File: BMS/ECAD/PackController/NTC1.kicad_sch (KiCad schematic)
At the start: 3 parts

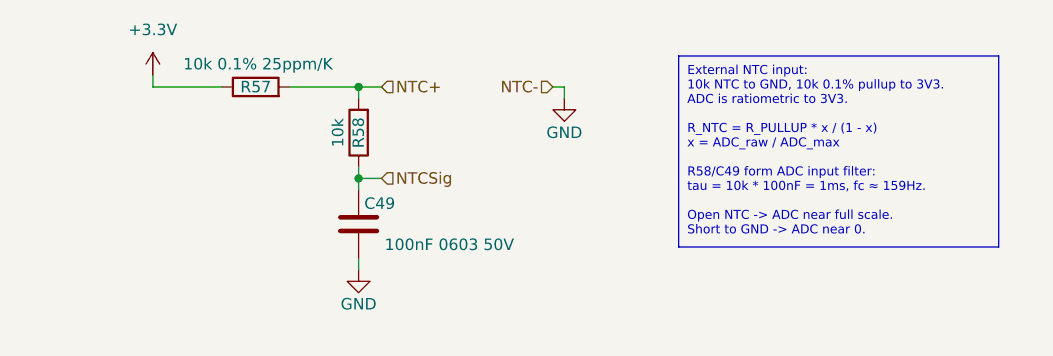
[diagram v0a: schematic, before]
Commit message: close to finish BMS master, only some footprints needed
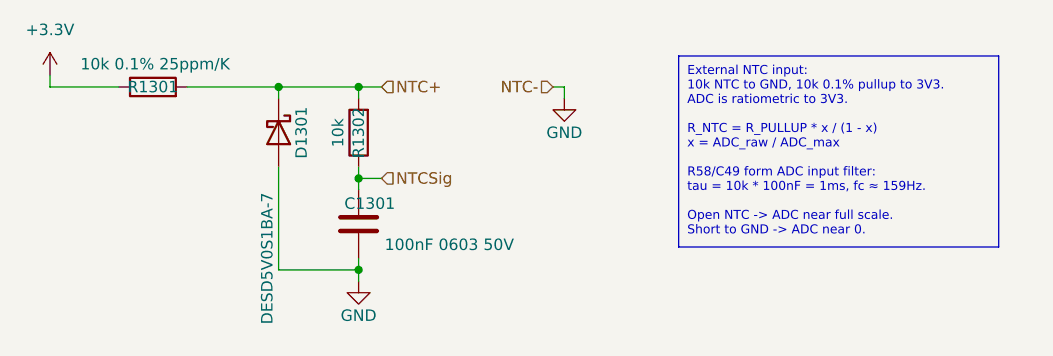
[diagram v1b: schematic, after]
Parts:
- added D1301: DESD5V0S1BA-7, Diode_SMD:D_SOD-323, symbol Device:D_Schottky
- renumbered C49 to C1301, R57 to R1301, R58 to R1302
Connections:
- net GND: now also D1301.2 (A)
- net NTC+: now also D1301.1 (K)
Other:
- moved on the sheet: R1301
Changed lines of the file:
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@@
+	)
+	(junction
+		(at 124.46 85.09)
+		(diameter 0)
+		(color 0 0 0 0)
 	)
 	(junction
@@
 		(color 0 0 0 0)
 	)
-	(wire
-		(pts
-			(xy 110.49 85.09) (xy 110.49 83.82)
+	(junction
+		(at 133.35 105.41)
+		(diameter 0)
+		(color 0 0 0 0)
+	)
+	(wire
+		(pts
+			(xy 99.06 85.09) (xy 99.06 83.82)
 		)
 		(stroke
@@
 	(wire
 		(pts
+			(xy 124.46 105.41) (xy 133.35 105.41)
+		)
+		(stroke
+			(width 0)
+			(type default)
+		)
+	)
+	(wire
+		(pts
+			(xy 124.46 85.09) (xy 124.46 86.36)
+		)
+		(stroke
+			(width 0)
+			(type default)
+		)
+	)
+	(wire
+		(pts
 			(xy 156.21 85.09) (xy 156.21 86.36)
 		)
@@
 	(wire
 		(pts
-			(xy 125.73 85.09) (xy 133.35 85.09)
+			(xy 124.46 85.09) (xy 133.35 85.09)
+		)
+		(stroke
+			(width 0)
+			(type default)
+		)
+	)
+	(wire
+		(pts
+			(xy 133.35 106.68) (xy 133.35 105.41)
+		)
+		(stroke
+			(width 0)
+			(type default)
+		)
+	)
+	(wire
+		(pts
+			(xy 114.3 85.09) (xy 124.46 85.09)
 		)
 		(stroke
@@
 	(wire
 		(pts
-			(xy 110.49 85.09) (xy 118.11 85.09)
+			(xy 124.46 93.98) (xy 124.46 105.41)
+		)
+		(stroke
+			(width 0)
+			(type default)
+		)
+	)
+	(wire
+		(pts
+			(xy 99.06 85.09) (xy 106.68 85.09)
 		)
 		(stroke
@@
 	(symbol
 		(lib_id "Device:R")
-		(at 121.92 85.09 90)
+		(at 110.49 85.09 90)
 		(unit 1)
 		(body_style 1)
@@
 		(in_pos_files yes)
 		(dnp no)
-		(property "Reference" "R57"
-			(at 121.92 85.09 90)
+		(property "Reference" "R1301"
+			(at 110.49 85.09 90)
 			(show_name no)
 			(do_not_autoplace no)
@@
 		)
 		(property "Value" "10k 0.1% 25ppm/K"
-			(at 122.174 82.55 90)
+			(at 110.744 82.55 90)
 			(show_name no)
 			(do_not_autoplace no)
@@
 		)
 		(property "Footprint" "Resistor_SMD:R_0603_1608Metric_Pad0.98x0.95mm_HandSolder"
-			(at 121.92 86.868 90)
+			(at 110.49 86.868 90)
 			(hide yes)
 			(show_name no)
@@
 		)
 		(property "Datasheet" ""
-			(at 121.92 85.09 0)
+			(at 110.49 85.09 0)
 			(hide yes)
 			(show_name no)
@@
 		)
 		(property "Description" ""
-			(at 121.92 85.09 0)
+			(at 110.49 85.09 0)
 			(show_name no)
 			(do_not_autoplace no)
@@
 			(project "Pack_Controller"
 				(path "/58a1c93e-baba-4d23-9191-955e00968735/45830960-bd48-4e73-a3a7-091edb18d6d3/71e65725-80b2-472c-8002-e08c907aa751"
-					(reference "R71")
+					(reference "R1401")
 					(unit 1)
 				)
 				(path "/58a1c93e-baba-4d23-9191-955e00968735/45830960-bd48-4e73-a3a7-091edb18d6d3/bb3a350a-a658-4971-83cd-58f1dca54bb5"
-					(reference "R73")
+					(reference "R1501")
 					(unit 1)
 				)
 				(path "/58a1c93e-baba-4d23-9191-955e00968735/45830960-bd48-4e73-a3a7-091edb18d6d3/f34c3682-d9f6-426f-8996-e47c99f84a0f"
-					(reference "R57")
+					(reference "R1301")
 					(unit 1)
 				)
@@
 		(in_pos_files yes)
 		(dnp no)
-		(property "Reference" "R58"
+		(property "Reference" "R1302"
 			(at 133.35 90.17 90)
 			(show_name no)
@@
 			(project "Pack_Controller"
 				(path "/58a1c93e-baba-4d23-9191-955e00968735/45830960-bd48-4e73-a3a7-091edb18d6d3/71e65725-80b2-472c-8002-e08c907aa751"
-					(reference "R72")
+					(reference "R1402")
 					(unit 1)
 				)
 				(path "/58a1c93e-baba-4d23-9191-955e00968735/45830960-bd48-4e73-a3a7-091edb18d6d3/bb3a350a-a658-4971-83cd-58f1dca54bb5"
-					(reference "R74")
+					(reference "R1502")
 					(unit 1)
 				)
 				(path "/58a1c93e-baba-4d23-9191-955e00968735/45830960-bd48-4e73-a3a7-091edb18d6d3/f34c3682-d9f6-426f-8996-e47c99f84a0f"
-					(reference "R58")
+					(reference "R1302")
 					(unit 1)
 				)
@@
 		(in_pos_files yes)
 		(dnp no)
-		(property "Reference" "C49"
+		(property "Reference" "C1301"
 			(at 137.414 98.044 0)
 			(show_name no)
@@
 			(project "Pack_Controller"
 				(path "/58a1c93e-baba-4d23-9191-955e00968735/45830960-bd48-4e73-a3a7-091edb18d6d3/71e65725-80b2-472c-8002-e08c907aa751"
-					(reference "C50")
+					(reference "C1401")
 					(unit 1)
 				)
 				(path "/58a1c93e-baba-4d23-9191-955e00968735/45830960-bd48-4e73-a3a7-091edb18d6d3/bb3a350a-a658-4971-83cd-58f1dca54bb5"
-					(reference "C51")
+					(reference "C1501")
 					(unit 1)
 				)
 				(path "/58a1c93e-baba-4d23-9191-955e00968735/45830960-bd48-4e73-a3a7-091edb18d6d3/f34c3682-d9f6-426f-8996-e47c99f84a0f"
-					(reference "C49")
+					(reference "C1301")
 					(unit 1)
 				)
@@
 	(symbol
 		(lib_id "power:GND")
-		(at 133.35 105.41 0)
+		(at 133.35 106.68 0)
 		(unit 1)
 		(body_style 1)
@@
 		(in_pos_files yes)
 		(dnp no)
-		(property "Reference" "#PWR061"
-			(at 133.35 111.76 0)
+		(property "Reference" "#PWR01303"
+			(at 133.35 113.03 0)
 			(hide yes)
 			(show_name no)
@@
 		)
 		(property "Value" "GND"
-			(at 133.35 109.22 0)
+			(at 133.35 110.49 0)
 			(show_name no)
 			(do_not_autoplace no)
@@
 		)
 		(property "Footprint" ""
-			(at 133.35 105.41 0)
+			(at 133.35 106.68 0)
 			(hide yes)
 			(show_name no)
@@
 		)
 		(property "Datasheet" ""
-			(at 133.35 105.41 0)
+			(at 133.35 106.68 0)
 			(hide yes)
 			(show_name no)
@@
 		)
 		(property "Description" ""
-			(at 133.35 105.41 0)
+			(at 133.35 106.68 0)
 			(show_name no)
 			(do_not_autoplace no)
@@
 			(project "Pack_Controller"
 				(path "/58a1c93e-baba-4d23-9191-955e00968735/45830960-bd48-4e73-a3a7-091edb18d6d3/71e65725-80b2-472c-8002-e08c907aa751"
-					(reference "#PWR063")
+					(reference "#PWR01403")
 					(unit 1)
 				)
 				(path "/58a1c93e-baba-4d23-9191-955e00968735/45830960-bd48-4e73-a3a7-091edb18d6d3/bb3a350a-a658-4971-83cd-58f1dca54bb5"
-					(reference "#PWR066")
+					(reference "#PWR01503")
 					(unit 1)
 				)
 				(path "/58a1c93e-baba-4d23-9191-955e00968735/45830960-bd48-4e73-a3a7-091edb18d6d3/f34c3682-d9f6-426f-8996-e47c99f84a0f"
-					(reference "#PWR061")
+					(reference "#PWR01303")
 					(unit 1)
 				)
@@
 	(symbol
 		(lib_id "power:+3.3V")
-		(at 110.49 83.82 0)
+		(at 99.06 83.82 0)
 		(unit 1)
 		(body_style 1)
@@
 		(dnp no)
 		(fields_autoplaced yes)
-		(property "Reference" "#PWR059"
-			(at 110.49 87.63 0)
+		(property "Reference" "#PWR01301"
+			(at 99.06 87.63 0)
 			(hide yes)
 			(show_name no)
@@
 		)
 		(property "Value" "+3.3V"
-			(at 110.49 78.74 0)
+			(at 99.06 78.74 0)
 			(show_name no)
 			(do_not_autoplace no)
@@
 		)
 		(property "Footprint" ""
-			(at 110.49 83.82 0)
+			(at 99.06 83.82 0)
 			(hide yes)
 			(show_name no)
@@
 		)
 		(property "Datasheet" ""
-			(at 110.49 83.82 0)
+			(at 99.06 83.82 0)
 			(hide yes)
 			(show_name no)
@@
 		)
 		(property "Description" ""
-			(at 110.49 83.82 0)
+			(at 99.06 83.82 0)
 			(show_name no)
 			(do_not_autoplace no)
@@
 			(project "Pack_Controller"
 				(path "/58a1c93e-baba-4d23-9191-955e00968735/45830960-bd48-4e73-a3a7-091edb18d6d3/71e65725-80b2-472c-8002-e08c907aa751"
-					(reference "#PWR062")
+					(reference "#PWR01401")
 					(unit 1)
 				)
 				(path "/58a1c93e-baba-4d23-9191-955e00968735/45830960-bd48-4e73-a3a7-091edb18d6d3/bb3a350a-a658-4971-83cd-58f1dca54bb5"
-					(reference "#PWR065")
+					(reference "#PWR01501")
 					(unit 1)
 				)
 				(path "/58a1c93e-baba-4d23-9191-955e00968735/45830960-bd48-4e73-a3a7-091edb18d6d3/f34c3682-d9f6-426f-8996-e47c99f84a0f"
-					(reference "#PWR059")
+					(reference "#PWR01301")
 					(unit 1)
 				)
@@
 		(in_pos_files yes)
 		(dnp no)
-		(property "Reference" "#PWR060"
+		(property "Reference" "#PWR01302"
 			(at 156.21 92.71 0)
 			(hide yes)
@@
 			(project "Pack_Controller"
 				(path "/58a1c93e-baba-4d23-9191-955e00968735/45830960-bd48-4e73-a3a7-091edb18d6d3/71e65725-80b2-472c-8002-e08c907aa751"
-					(reference "#PWR064")
+					(reference "#PWR01402")
 					(unit 1)
 				)
 				(path "/58a1c93e-baba-4d23-9191-955e00968735/45830960-bd48-4e73-a3a7-091edb18d6d3/bb3a350a-a658-4971-83cd-58f1dca54bb5"
-					(reference "#PWR067")
+					(reference "#PWR01502")
 					(unit 1)
 				)
 				(path "/58a1c93e-baba-4d23-9191-955e00968735/45830960-bd48-4e73-a3a7-091edb18d6d3/f34c3682-d9f6-426f-8996-e47c99f84a0f"
-					(reference "#PWR060")
-					(unit 1)
-				)
+					(reference "#PWR01302")
+					(unit 1)
+				)
+			)
+		)
+	)
+	(symbol
+		(lib_id "Device:D_Schottky")
+		(at 124.46 90.17 270)
+		(unit 1)
+		(body_style 1)
+		(exclude_from_sim no)
+		(in_bom yes)
+		(on_board yes)
+		(in_pos_files yes)
+		(dnp no)
+		(property "Reference" "D1301"
+			(at 127 90.17 0)
+			(show_name no)
+			(do_not_autoplace no)
+			(effects
+				(font
+					(size 1.27 1.27)
+				)
+			)
+		)
+		(property "Value" "DESD5V0S1BA-7"
+			(at 123.19 104.14 0)
+			(show_name no)
+			(do_not_autoplace no)
+			(effects
+				(font
+					(size 1.27 1.27)
+				)
+			)
+		)
+		(property "Footprint" "Diode_SMD:D_SOD-323"
+			(at 124.46 90.17 0)
+			(hide yes)
+			(show_name no)
+			(do_not_autoplace no)
+			(effects
+				(font
+					(size 1.27 1.27)
+				)
+			)
+		)
+		(property "Datasheet" ""
+			(at 124.46 90.17 0)
+			(hide yes)
+			(show_name no)
+			(do_not_autoplace no)
+			(effects
+				(font
+					(size 1.27 1.27)
+				)
+			)
+		)
+		(property "Description" ""
+			(at 124.46 90.17 0)
+			(show_name no)
+			(do_not_autoplace no)
+			(effects
+				(font
+					(size 1.27 1.27)
+				)
+			)
+		)
+		(pin "2"
+		)
+		(pin "1"
+		)
+		(instances
+			(project "Pack_Controller"
+				(path "/58a1c93e-baba-4d23-9191-955e00968735/45830960-bd48-4e73-a3a7-091edb18d6d3/71e65725-80b2-472c-8002-e08c907aa751"
+					(reference "D1401")
+					(unit 1)
+				)
+				(path "/58a1c93e-baba-4d23-9191-955e00968735/45830960-bd48-4e73-a3a7-091edb18d6d3/bb3a350a-a658-4971-83cd-58f1dca54bb5"
+					(reference "D1501")
+					(unit 1)
+				)
+				(path "/58a1c93e-baba-4d23-9191-955e00968735/45830960-bd48-4e73-a3a7-091edb18d6d3/f34c3682-d9f6-426f-8996-e47c99f84a0f"
+					(reference "D1301")
+					(unit 1)
+				)

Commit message: yes
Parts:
- D1301: symbol Device:D_Schottky -> Device:D_TVS
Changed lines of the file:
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@@
 	)
 	(symbol
-		(lib_id "Device:D_Schottky")
+		(lib_id "Device:D_TVS")
 		(at 124.46 90.17 270)
 		(unit 1)
@@
 			)
 		)
-		(property "Description" ""
+		(property "Description" "Bidirectional transient-voltage-suppression diode"
 			(at 124.46 90.17 0)
+			(hide yes)
 			(show_name no)
 			(do_not_autoplace no)
